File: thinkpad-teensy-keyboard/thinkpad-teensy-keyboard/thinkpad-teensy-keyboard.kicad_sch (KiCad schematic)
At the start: 16 parts

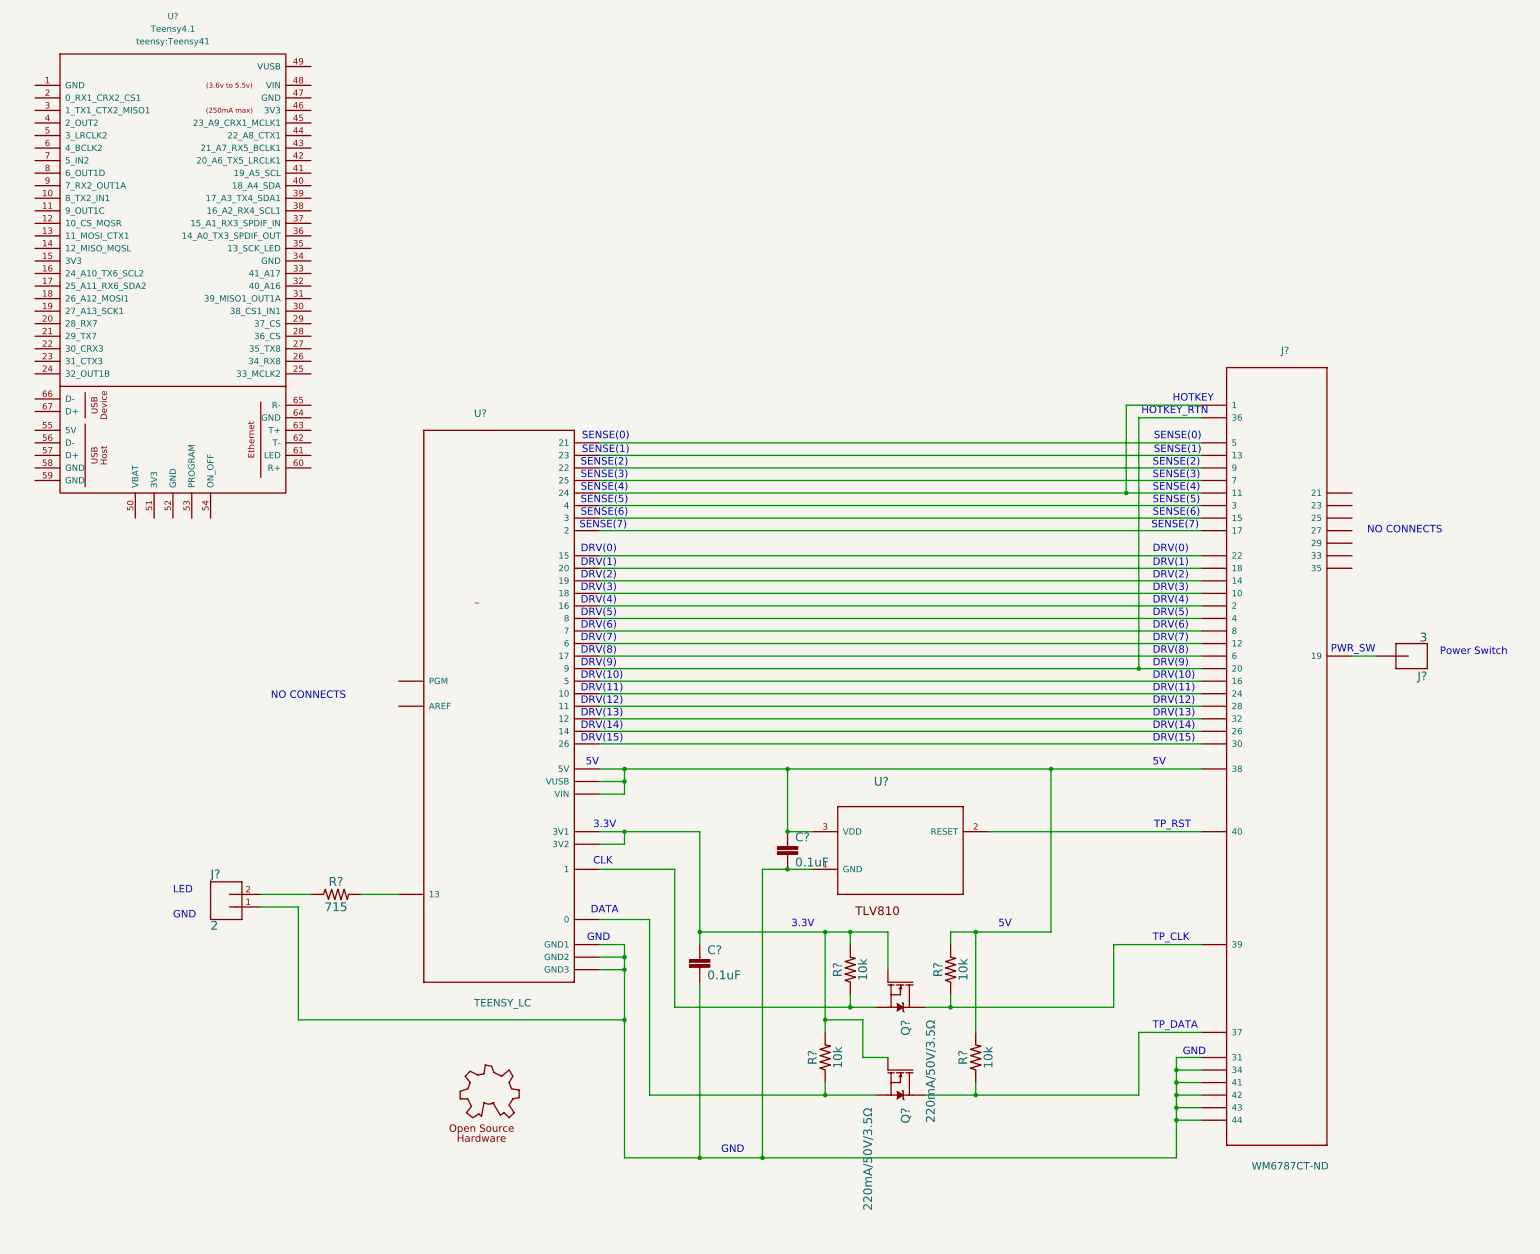
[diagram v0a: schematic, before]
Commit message: Schematic updates
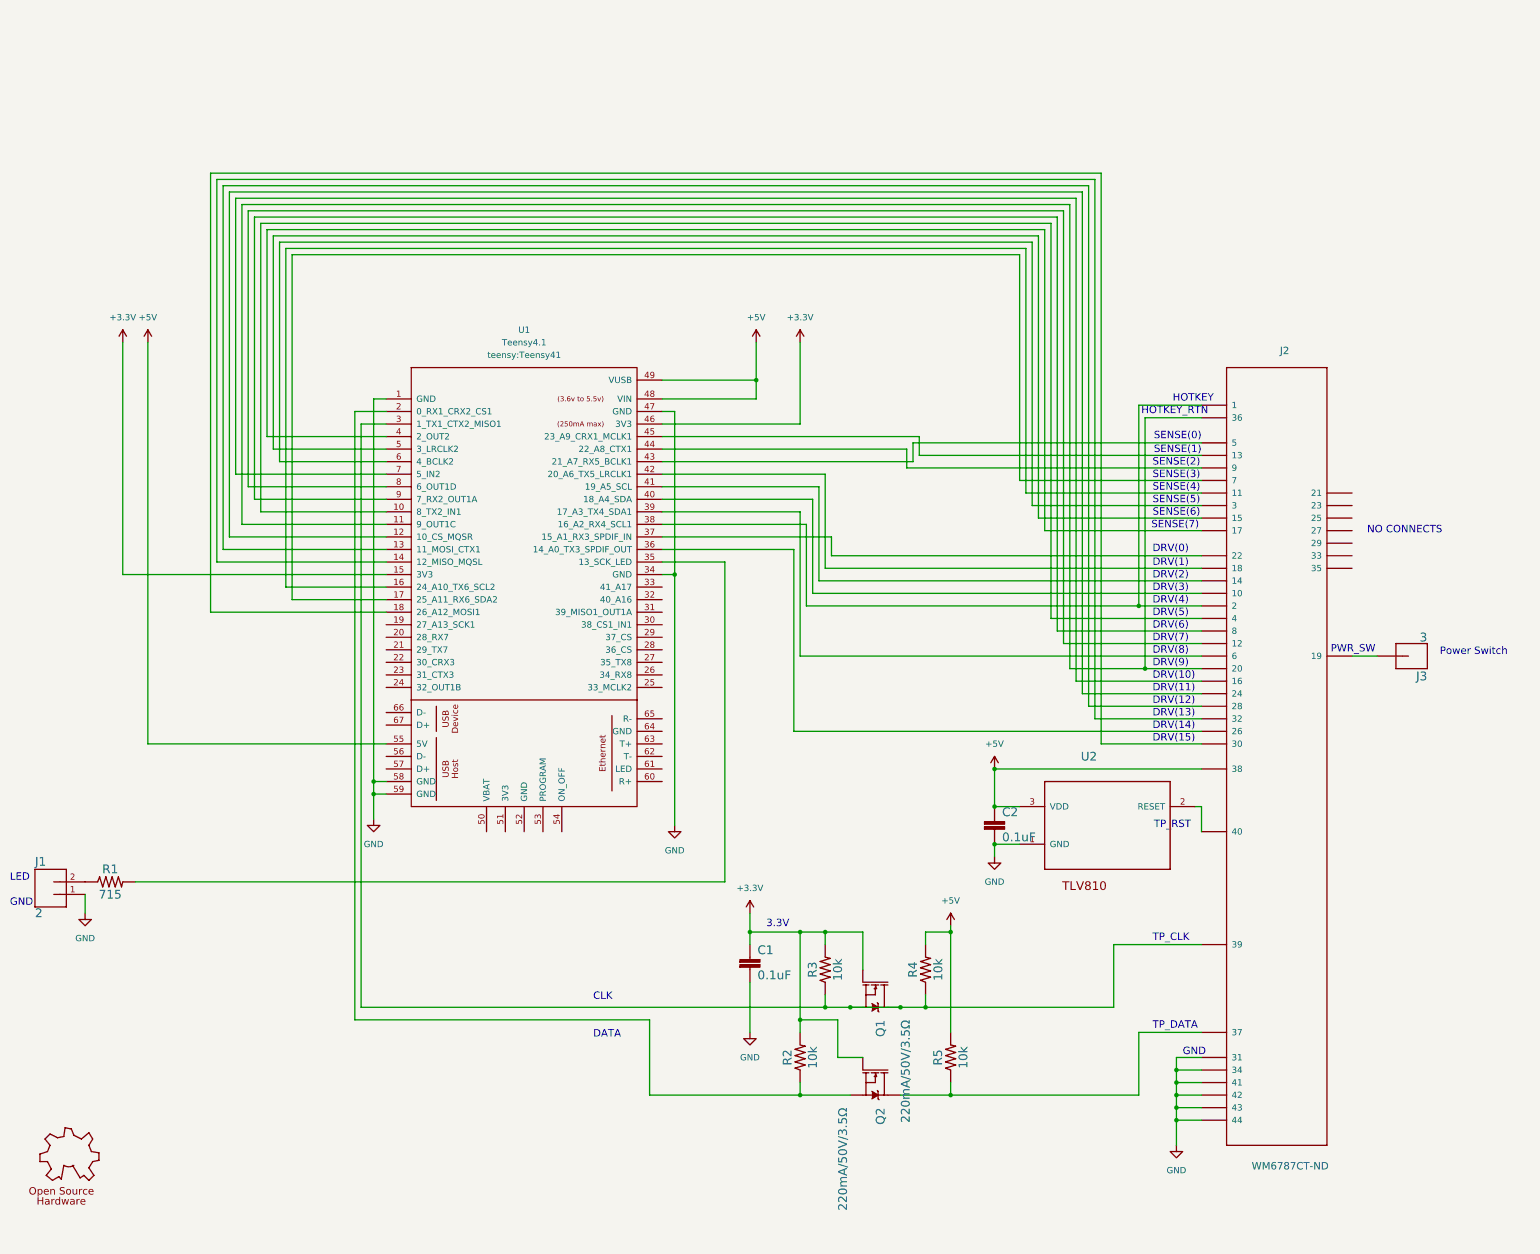
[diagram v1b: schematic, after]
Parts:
- removed U?: TEENSY_LC, T61_LC_Scanner:TEENSY_LC, symbol T61_LC_Scanner-eagle-import:TEENSY_LC
- gave numbers to parts that had none: 15
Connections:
- net +5V: now reaches C2.1, J2.P$38 (38), R4.2, R5.2, U2.3 (VDD)
- net +5V: now also U1.48 (VIN), U1.49 (VUSB), U1.55 (5V)
- net GND: now reaches C1.2, C2.2, J1.1, J2.P$31 (31), J2.P$34 (34), J2.P$41 (43), J2.P$42 (44), J2.P$43 (41), J2.P$44 (42), U2.1 (GND)
- net GND: now also U1.1 (GND), U1.34 (GND), U1.47 (GND), U1.58 (GND), U1.59 (GND)
- net +3V3: now reaches C1.1, Q1.1 (G), Q2.1 (G), R2.2, R3.2
- net +3V3: now also U1.15 (3V3), U1.46 (3V3)
- net at Q1.2 (S), R3.1: now also J2.P$39 (39), Q1.3 (D), R4.1, U1.3 (1_TX1_CTX2_MISO1)
- net at U1.10 (8_TX2_IN1): now also J2.P$4 (4)
- net at U1.11 (9_OUT1C): now also J2.P$20 (20), J2.P$36 (36)
- net at U1.12 (10_CS_MQSR): now also J2.P$24 (24)
- net at U1.13 (11_MOSI_CTX1): now also J2.P$28 (28)
- net at U1.14 (12_MISO_MQSL): now also J2.P$32 (32)
- net at U1.16 (24_A10_TX6_SCL2): now also J2.P$11 (11)
- net at U1.17 (25_A11_RX6_SDA2): now also J2.P$7 (7)
- net at U1.18 (26_A12_MOSI1): now also J2.P$30 (30)
- net at U1.2 (0_RX1_CRX2_CS1): now also Q2.2 (S), R2.1
- net at U1.35 (13_SCK_LED): now also R1.2
- net at U1.36 (14_A0_TX3_SPDIF_OUT): now also J2.P$26 (26)
- net at U1.37 (15_A1_RX3_SPDIF_IN): now also J2.P$22 (22)
- net at U1.38 (16_A2_RX4_SCL1): now also J2.P$1 (1), J2.P$2 (2)
- net at U1.39 (17_A3_TX4_SDA1): now also J2.P$6 (6)
- net at U1.4 (2_OUT2): now also J2.P$17 (17)
- net at U1.40 (18_A4_SDA): now also J2.P$10 (10)
- net at U1.41 (19_A5_SCL): now also J2.P$14 (14)
- net at U1.42 (20_A6_TX5_LRCLK1): now also J2.P$18 (18)
- net at U1.43 (21_A7_RX5_BCLK1): now also J2.P$5 (5)
- net at U1.44 (22_A8_CTX1): now also J2.P$9 (9)
- net at U1.45 (23_A9_CRX1_MCLK1): now also J2.P$13 (13)
- net at U1.5 (3_LRCLK2): now also J2.P$15 (15)
- net at U1.6 (4_BCLK2): now also J2.P$3 (3)
- net at U1.7 (5_IN2): now also J2.P$16 (16)
- net at U1.8 (6_OUT1D): now also J2.P$12 (12)
- net at U1.9 (7_RX2_OUT1A): now also J2.P$8 (8)
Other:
- note removed: "5V"
- moved on the sheet: C1, C2, J1, Q1, Q2, R1, R2, R3, R4, R5, U1, U2

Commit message: updates
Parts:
- removed C2: 0.1uF, T61_LC_Scanner:0603, symbol T61_LC_Scanner-eagle-import:0.1UF-0603-25V-(+80_-20%)
- removed J1: 2, T61_LC_Scanner:1X02, symbol T61_LC_Scanner-eagle-import:CONN_02
- removed R1: 715, T61_LC_Scanner:0603, symbol T61_LC_Scanner-eagle-import:715OHM-0603-1_10W-1%
- removed U2: TLV810SDBZT, T61_LC_Scanner:SOT95P237X112-3N, symbol T61_LC_Scanner-eagle-import:TLV810SDBZT
- C1, R2, R3, R4, R5: footprint T61_LC_Scanner:0603 -> Library:0603
- GOLD_ORB_SM1: footprint T61_LC_Scanner:OSHW_5MM -> Library:OSHW_5MM
- J2: footprint T61_LC_Scanner:WM6787CT-ND -> Library:WM6787CT-ND
- J3: footprint T61_LC_Scanner:1X01 -> Library:1X01
- Q1, Q2: footprint T61_LC_Scanner:SOT23-3 -> Library:SOT23-3
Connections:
- net at U1.10 (8_TX2_IN1): now also J2.P$13 (13); no longer J2.P$4 (4)
- net at U1.12 (10_CS_MQSR): now also J2.P$36 (36); no longer J2.P$24 (24)
- net at U1.13 (11_MOSI_CTX1): now also J2.P$1 (1); no longer J2.P$28 (28)
- net at U1.14 (12_MISO_MQSL): no longer J2.P$32 (32)
- net at U1.16 (24_A10_TX6_SCL2): no longer J2.P$11 (11)
- net at U1.17 (25_A11_RX6_SDA2): no longer J2.P$7 (7)
- net at U1.18 (26_A12_MOSI1): no longer J2.P$30 (30)
- net at U1.28 (36_CS): now also J2.P$40 (40)
- net at U1.29 (37_CS): now also J2.P$30 (30)
- net at U1.30 (38_CS1_IN1): now also J2.P$26 (26)
- net at U1.31 (39_MISO1_OUT1A): now also J2.P$32 (32)
- net at U1.32 (40_A16): now also J2.P$28 (28)
- net at U1.33 (41_A17): now also J2.P$24 (24)
- net at U1.35 (13_SCK_LED): now also J2.P$16 (16)
- net at U1.36 (14_A0_TX3_SPDIF_OUT): now also J2.P$20 (20); no longer J2.P$26 (26)
- net at U1.37 (15_A1_RX3_SPDIF_IN): now also J2.P$6 (6); no longer J2.P$22 (22)
- net at U1.39 (17_A3_TX4_SDA1): now also J2.P$8 (8); no longer J2.P$6 (6)
- net at U1.40 (18_A4_SDA): now also J2.P$4 (4); no longer J2.P$10 (10)
- net at U1.41 (19_A5_SCL): now also J2.P$2 (2); no longer J2.P$14 (14)
- net at U1.42 (20_A6_TX5_LRCLK1): now also J2.P$10 (10); no longer J2.P$18 (18)
- net at J2.P$5 (5): now also U1.11 (9_OUT1C); no longer U1.43 (21_A7_RX5_BCLK1)
- net at U1.44 (22_A8_CTX1): now also J2.P$18 (18); no longer J2.P$9 (9)
- net at U1.45 (23_A9_CRX1_MCLK1): now also J2.P$22 (22); no longer J2.P$13 (13)
- net at U1.7 (5_IN2): now also J2.P$11 (11); no longer J2.P$16 (16)
- net at J2.P$12 (12): now also U1.38 (16_A2_RX4_SCL1); no longer U1.8 (6_OUT1D)
- net at U1.9 (7_RX2_OUT1A): now also J2.P$9 (9); no longer J2.P$8 (8)
- new net: J2.P$14 (14), U1.43 (21_A7_RX5_BCLK1)
- new net: J2.P$7 (7), U1.8 (6_OUT1D)
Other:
- note removed: "LED"

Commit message: Generated Gerbers
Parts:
- removed J3: 3, Library:1X01, symbol T61_LC_Scanner-eagle-import:CONN_01
- U1: footprint teensy:Teensy41 -> teensy:Teensy41_ignore_ethernet
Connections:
- net at Q1.2 (S), R3.1, U1.3 (1_TX1_CTX2_MISO1): no longer J2.P$39 (39), Q1.3 (D), R4.1
- net at U1.10 (8_TX2_IN1): now also J2.P$24 (24); no longer J2.P$13 (13)
- net at U1.11 (9_OUT1C): now also J2.P$22 (22); no longer J2.P$5 (5)
- net at U1.12 (10_CS_MQSR): now also J2.P$20 (20); no longer J2.P$36 (36)
- net at U1.13 (11_MOSI_CTX1): now also J2.P$18 (18); no longer J2.P$1 (1)
- net at U1.14 (12_MISO_MQSL): now also J2.P$16 (16)
- net at U1.16 (24_A10_TX6_SCL2): now also J2.P$14 (14)
- net at U1.17 (25_A11_RX6_SDA2): now also J2.P$12 (12)
- net at U1.18 (26_A12_MOSI1): now also J2.P$10 (10)
- net at U1.28 (36_CS): no longer J2.P$40 (40)
- net at U1.29 (37_CS): no longer J2.P$30 (30)
- net at U1.30 (38_CS1_IN1): no longer J2.P$26 (26)
- net at U1.31 (39_MISO1_OUT1A): now also J2.P$19 (19); no longer J2.P$32 (32)
- net at U1.32 (40_A16): now also J2.P$4 (4); no longer J2.P$28 (28)
- net at U1.33 (41_A17): now also J2.P$2 (2); no longer J2.P$24 (24)
- net at U1.35 (13_SCK_LED): now also J2.P$6 (6); no longer J2.P$16 (16)
- net at U1.36 (14_A0_TX3_SPDIF_OUT): now also J2.P$8 (8); no longer J2.P$20 (20)
- net at U1.37 (15_A1_RX3_SPDIF_IN): now also J2.P$1 (1); no longer J2.P$6 (6)
- net at U1.38 (16_A2_RX4_SCL1): now also J2.P$3 (3); no longer J2.P$12 (12)
- net at U1.39 (17_A3_TX4_SDA1): now also J2.P$5 (5); no longer J2.P$8 (8)
- net at U1.4 (2_OUT2): now also J2.P$40 (40); no longer J2.P$17 (17)
- net at U1.40 (18_A4_SDA): now also J2.P$7 (7); no longer J2.P$4 (4)
- net at U1.41 (19_A5_SCL): now also J2.P$9 (9); no longer J2.P$2 (2)
- net at U1.42 (20_A6_TX5_LRCLK1): now also J2.P$11 (11); no longer J2.P$10 (10)
- net at U1.43 (21_A7_RX5_BCLK1): now also J2.P$13 (13); no longer J2.P$14 (14)
- net at U1.44 (22_A8_CTX1): now also J2.P$15 (15); no longer J2.P$18 (18)
- net at U1.45 (23_A9_CRX1_MCLK1): now also J2.P$17 (17); no longer J2.P$22 (22)
- net at U1.5 (3_LRCLK2): now also J2.P$36 (36); no longer J2.P$15 (15)
- net at U1.6 (4_BCLK2): now also J2.P$32 (32); no longer J2.P$3 (3)
- net at U1.7 (5_IN2): now also J2.P$30 (30); no longer J2.P$11 (11)
- net at U1.8 (6_OUT1D): now also J2.P$28 (28); no longer J2.P$7 (7)
- net at U1.9 (7_RX2_OUT1A): now also J2.P$26 (26); no longer J2.P$9 (9)
- new net: J2.P$39 (39), Q1.3 (D), R4.1
